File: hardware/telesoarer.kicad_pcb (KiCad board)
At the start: 4 copper layers, 50.3 x 19.1 mm, 52 parts, among them IC1 STM32F103CBT6, J1 BOOT0, J2 RESET, K1 RC_SIG, P1 PZ, P2 PZ_IN, P3 OLED 0.91" 128x32, P4 AOUT, P5 CONN_01X05, Q1 BC847C, U1 MS5611, U2 MCP1703T-3302, U3 AD8027ARTZ, X1 16MHz

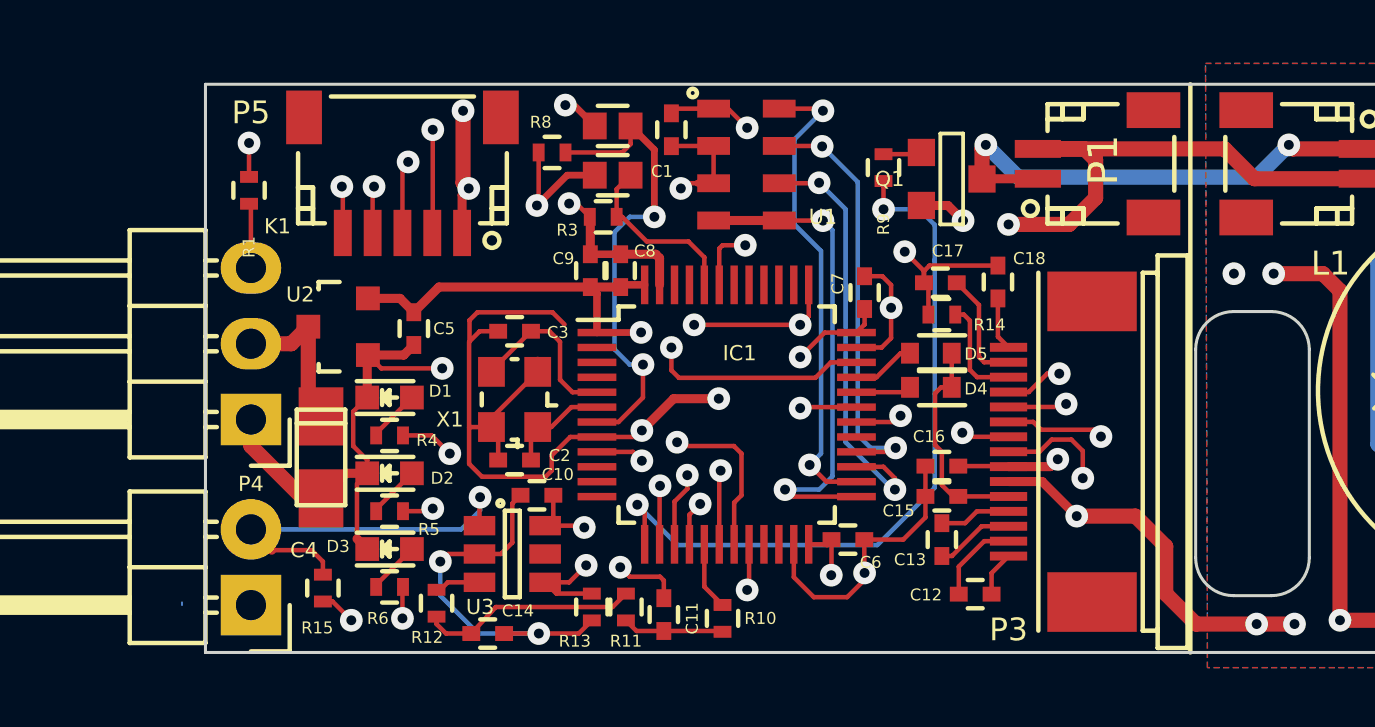
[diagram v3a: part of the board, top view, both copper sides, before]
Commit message: Oscillator Keep-out and GND shield changes
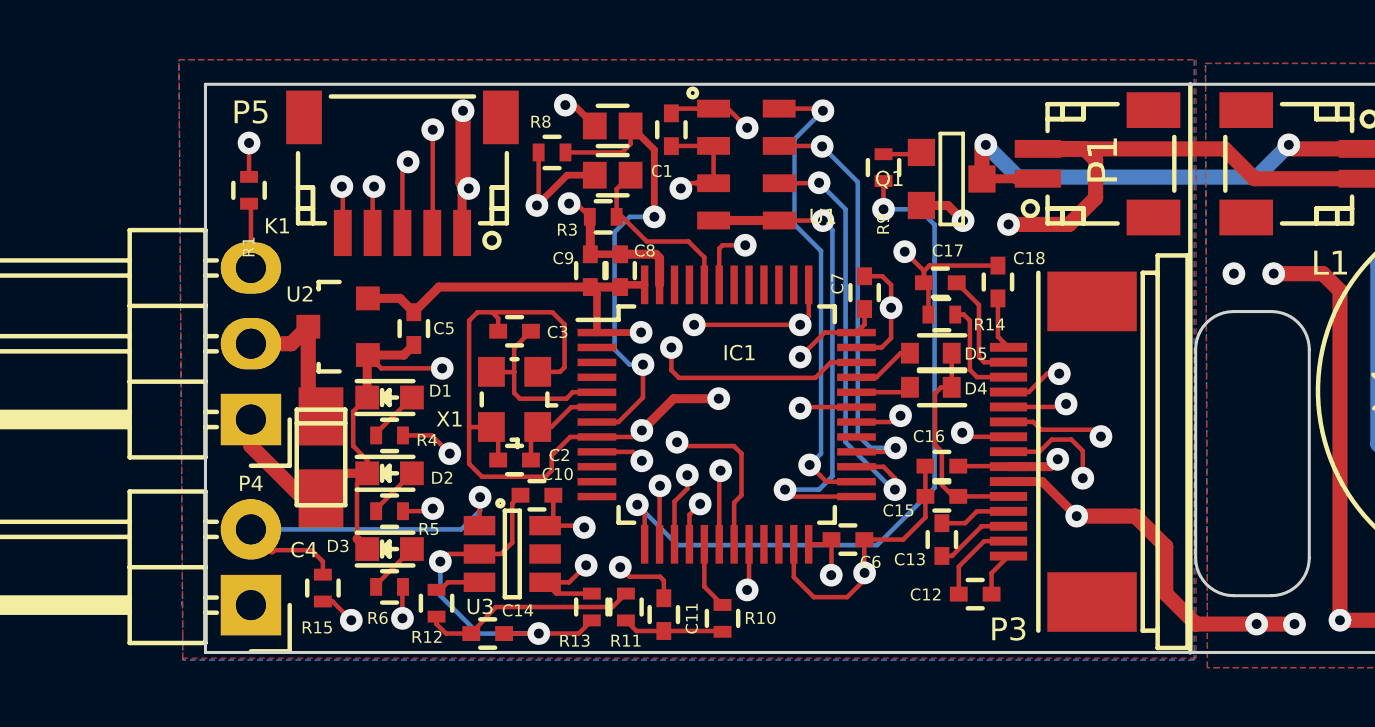
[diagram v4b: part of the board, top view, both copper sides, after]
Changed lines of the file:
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@@
     (thickness 1.6)
     (drawings 33)
-    (tracks 588)
+    (tracks 595)
     (zones 0)
     (modules 52)
@@
   (segment (start 26.924 31.5595) (end 26.924 29.4695) (width 0.1524) (layer F.Cu) (net 4))
   (segment (start 26.924 29.4695) (end 26.8605 29.406) (width 0.1524) (layer F.Cu) (net 4))
+  (segment (start 37.4396 33.4518) (end 37.4396 34.8869) (width 0.1524) (layer F.Cu) (net 5))
+  (segment (start 37.0332 33.0454) (end 37.4396 33.4518) (width 0.1524) (layer F.Cu) (net 5) (status 40000))
+  (segment (start 37.0205 33.0454) (end 37.0332 33.0454) (width 0.1524) (layer F.Cu) (net 5) (status 40000))
+  (segment (start 35.0139 33.0454) (end 37.0205 33.0454) (width 0.1524) (layer F.Cu) (net 5) (status 40000))
+  (segment (start 37.2851 35.0414) (end 36.5382 35.0414) (width 0.1524) (layer F.Cu) (net 5) (status 800000))
+  (segment (start 37.4396 34.8869) (end 37.2851 35.0414) (width 0.1524) (layer F.Cu) (net 5))
+  (segment (start 35.2132 33.6804) (end 35.2132 33.2447) (width 0.1524) (layer F.Cu) (net 5) (status 400000))
+  (segment (start 35.2132 33.2447) (end 35.0139 33.0454) (width 0.1524) (layer F.Cu) (net 5))
+  (segment (start 34.2392 36.8935) (end 34.2392 33.3248) (width 0.1524) (layer F.Cu) (net 5))
+  (segment (start 34.2519 33.3121) (end 34.5186 33.0454) (width 0.1524) (layer F.Cu) (net 5) (status 40000))
+  (segment (start 34.5186 33.0454) (end 35.0139 33.0454) (width 0.1524) (layer F.Cu) (net 5) (status 40000))
+  (segment (start 34.2392 33.3248) (end 34.2519 33.3121) (width 0.1524) (layer F.Cu) (net 5))
   (segment (start 61.214 31.75) (end 61.214 30.9245) (width 0.508) (layer In1.Cu) (net 5))
   (via (at 65.659 26.4795) (size 0.762) (drill 0.3302) (layers F.Cu B.Cu) (net 5))
@@
   (segment (start 49.5388 39.92) (end 48.7934 40.6654) (width 0.1524) (layer F.Cu) (net 5))
   (segment (start 48.7934 40.6654) (end 47.4892 40.6654) (width 0.1524) (layer F.Cu) (net 5))
-  (segment (start 34.2519 34.0233) (end 34.2519 33.3121) (width 0.1524) (layer F.Cu) (net 5) (status 40000))
-  (segment (start 37.0332 33.0454) (end 37.4396 33.4518) (width 0.1524) (layer F.Cu) (net 5) (status 40000))
-  (segment (start 34.5186 33.0454) (end 37.0332 33.0454) (width 0.1524) (layer F.Cu) (net 5) (status 40000))
-  (segment (start 34.2519 33.3121) (end 34.5186 33.0454) (width 0.1524) (layer F.Cu) (net 5) (status 40000))
   (segment (start 34.9882 36.8914) (end 34.9882 36.5914) (width 0.1524) (layer F.Cu) (net 5) (status 30))
-  (segment (start 34.9882 36.5914) (end 36.5382 35.0414) (width 0.1524) (layer F.Cu) (net 5) (status 30))
   (segment (start 34.2392 36.8935) (end 34.9861 36.8935) (width 0.1524) (layer F.Cu) (net 5) (status 20))
   (segment (start 34.9861 36.8935) (end 34.9882 36.8914) (width 0.1524) (layer F.Cu) (net 5) (status 30))
@@
   (segment (start 42.4356 27.4674) (end 42.4356 28.7174) (width 0.1524) (layer F.Cu) (net 5) (status 30))
   (segment (start 36.5382 35.3414) (end 36.5382 35.0414) (width 0.1524) (layer F.Cu) (net 5) (status 30))
-  (segment (start 34.2392 34.036) (end 34.2519 34.0233) (width 0.1524) (layer F.Cu) (net 5))
-  (segment (start 34.2519 34.0233) (end 34.5948 33.6804) (width 0.1524) (layer F.Cu) (net 5))
   (segment (start 34.2392 38.1254) (end 34.2392 36.8935) (width 0.1524) (layer F.Cu) (net 5))
-  (segment (start 34.2392 36.8935) (end 34.2392 34.036) (width 0.1524) (layer F.Cu) (net 5))
   (segment (start 38.5252 37.2244) (end 37.6294 37.2244) (width 0.1524) (layer F.Cu) (net 5) (status 10))
   (segment (start 36.8046 38.5572) (end 34.671 38.5572) (width 0.1524) (layer F.Cu) (net 5))
@@
   (segment (start 37.6294 37.2244) (end 37.0078 37.846) (width 0.1524) (layer F.Cu) (net 5))
   (segment (start 34.671 38.5572) (end 34.2392 38.1254) (width 0.1524) (layer F.Cu) (net 5))
-  (segment (start 34.5948 33.6804) (end 35.2132 33.6804) (width 0.1524) (layer F.Cu) (net 5) (status 20))
   (segment (start 34.9882 36.8914) (end 34.9882 36.716) (width 0.1524) (layer F.Cu) (net 5) (status 30))
   (segment (start 36.5382 35.0414) (end 36.5382 34.6072) (width 0.1524) (layer F.Cu) (net 5) (status 30))
@@
   (segment (start 37.6642 36.2244) (end 38.5252 36.2244) (width 0.1524) (layer F.Cu) (net 22) (status 20))
   (segment (start 36.9972 36.8914) (end 37.6642 36.2244) (width 0.1524) (layer F.Cu) (net 22))
-  (segment (start 38.5252 35.7244) (end 37.7056 35.7244) (width 0.1524) (layer F.Cu) (net 23) (status 10))
-  (segment (start 36.9316 33.6804) (end 36.3132 33.6804) (width 0.1524) (layer F.Cu) (net 23) (status 20))
-  (segment (start 37.2872 34.036) (end 36.9316 33.6804) (width 0.1524) (layer F.Cu) (net 23))
-  (segment (start 37.2872 35.306) (end 37.2872 34.036) (width 0.1524) (layer F.Cu) (net 23))
-  (segment (start 37.7056 35.7244) (end 37.2872 35.306) (width 0.1524) (layer F.Cu) (net 23))
-  (segment (start 36.3132 33.6804) (end 34.9882 35.0054) (width 0.1524) (layer F.Cu) (net 23) (status 30))
+  (segment (start 35.7505 35.052) (end 34.9988 35.052) (width 0.1524) (layer F.Cu) (net 23) (status 800000))
+  (segment (start 34.9988 35.052) (end 34.9882 35.0414) (width 0.1524) (layer F.Cu) (net 23) (status C00000))
+  (segment (start 37.719 35.7244) (end 37.5024 35.941) (width 0.1524) (layer F.Cu) (net 23))
+  (segment (start 35.7505 34.2431) (end 36.3132 33.6804) (width 0.1524) (layer F.Cu) (net 23) (status 800000))
+  (segment (start 35.7505 35.7505) (end 35.7505 35.052) (width 0.1524) (layer F.Cu) (net 23))
+  (segment (start 35.7505 35.052) (end 35.7505 34.2431) (width 0.1524) (layer F.Cu) (net 23))
+  (segment (start 35.941 35.941) (end 35.7505 35.7505) (width 0.1524) (layer F.Cu) (net 23))
+  (segment (start 37.5024 35.941) (end 35.941 35.941) (width 0.1524) (layer F.Cu) (net 23))
+  (segment (start 38.5252 35.7244) (end 37.719 35.7244) (width 0.1524) (layer F.Cu) (net 23) (status 10))
+  (segment (start 37.719 35.7244) (end 37.7056 35.7244) (width 0.1524) (layer F.Cu) (net 23) (status 10))
   (segment (start 34.9882 35.0054) (end 34.9882 35.0414) (width 0.1524) (layer F.Cu) (net 23) (status 30))
   (segment (start 34.9882 35.3184) (end 34.9882 35.0414) (width 0.1524) (layer F.Cu) (net 23) (status 30))
@@
     (polygon
       (pts
-        (xy 34.1122 32.9946) (xy 37.6428 32.9946) (xy 37.6428 38.7096) (xy 34.1122 38.7096)
+        (xy 33.9217 32.6771) (xy 37.5793 32.6771) (xy 37.6428 38.7731) (xy 33.9852 38.7731)
       )
     )
@@
     )
   )
-  (zone (net 0) (net_name "") (layer B.Cu) (hatch full 0.508)
-    (connect_pads (clearance 0.508))
-    (min_thickness 0.254)
-    (keepout (tracks not_allowed) (vias not_allowed) (copperpour not_allowed))
-    (fill (arc_segments 16) (thermal_gap 0.508) (thermal_bridge_width 0.508))
-    (polygon
-      (pts
-        (xy 37.6428 38.7096) (xy 34.1122 38.7096) (xy 34.1122 32.9946) (xy 37.6428 32.9946)
-      )
-    )
-  )
   (zone (net 15) (net_name +3V3) (layer In1.Cu) (hatch edge 0.508)
     (connect_pads (clearance 0.254))
@@
     )
   )
-  (zone (net 0) (net_name "") (layer In1.Cu) (hatch edge 0.508)
-    (connect_pads (clearance 0.254))
-    (min_thickness 0.254)
-    (keepout (tracks not_allowed) (vias not_allowed) (copperpour not_allowed))
-    (fill (arc_segments 16) (thermal_gap 0.381) (thermal_bridge_width 0.381))
-    (polygon
-      (pts
-        (xy 34.1122 32.9946) (xy 37.6428 32.9946) (xy 37.6428 38.7096) (xy 34.1122 38.7096) (xy 34.1122 35.5854)
-      )
-    )
-  )
   (zone (net 0) (net_name "") (layer In2.Cu) (hatch edge 0.508)
     (connect_pads (clearance 0.254))
@@
     (polygon
       (pts
-        (xy 37.6428 38.7096) (xy 34.1122 38.7096) (xy 34.1122 32.9946) (xy 37.6428 32.9946)
+        (xy 37.6428 38.7731) (xy 33.9852 38.7731) (xy 33.9217 32.6771) (xy 37.5793 32.6771)
       )
     )
@@
       )
     )
+  )
+  (zone (net 5) (net_name GND) (layer F.Cu) (hatch edge 0.508)
+    (connect_pads (clearance 0.254))
+    (min_thickness 0.254)
+    (fill yes (arc_segments 16) (thermal_gap 0.381) (thermal_bridge_width 0.381))
+    (polygon
+      (pts
+        (xy 24.511 24.5745) (xy 58.6105 24.5745) (xy 58.6105 44.6405) (xy 24.638 44.6405) (xy 24.638 43.8785)
+      )
+    )
+  )
+  (zone (net 5) (net_name GND) (layer B.Cu) (hatch edge 0.508)
+    (connect_pads (clearance 0.254))
+    (min_thickness 0.254)
+    (fill yes (arc_segments 16) (thermal_gap 0.381) (thermal_bridge_width 0.381))
+    (polygon
+      (pts
+        (xy 24.511 24.5745) (xy 58.547 24.5745) (xy 58.547 44.704) (xy 24.638 44.704) (xy 24.638 43.942)
+      )
+    )
+  )
+  (zone (net 0) (net_name "") (layer In1.Cu) (hatch edge 0.508)
+    (connect_pads (clearance 0.254))
+    (min_thickness 0.254)
+    (keepout (tracks not_allowed) (vias not_allowed) (copperpour not_allowed))
+    (fill (arc_segments 16) (thermal_gap 0.381) (thermal_bridge_width 0.381))
+    (polygon
+      (pts
+        (xy 33.9725 32.639) (xy 37.6555 32.639) (xy 37.6555 38.7985) (xy 33.9725 38.7985) (xy 33.9725 38.735)
+      )
+    )
